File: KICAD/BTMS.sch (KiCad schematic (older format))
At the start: 314 parts, among them J1 fan, J10 U1COMMS, J11 U2COMMS, J13 IntBTemp, J14 ctrlTemp, J15 12Vout, J16 12Vin, J17 5Vout, J2 mContactor, J3 Tac, J5 ICSP, J7 5Vout, J9 key, Q1 PSMN5R6-100BS, Q10 PSMN5R6-100BS, Q11 DMN65D8L, Q12 DMN65D8L, Q13 FDN340P, Q14 ZXTP2025FTA, Q15 ZXTP2025FTA, Q16 ZXTP2025FTA, Q18 DMN65D8L, Q2 PSMN5R6-100BS, Q3 PSMN5R6-100BS, Q4 DMN65D8L, Q5 DMN65D8L, Q6 DMN65D8L, Q7 DMN65D8L, Q8 PSMN5R6-100BS, Q9 FDN340P, U1 R-78HB12-0.5, U10 A41AS12VDC, U11 A41AS12VDC, U12 A41AS12VDC, U13 A41AS12VDC, U14 A41AS12VDC, U15 NL17SZ74USG, U2 ACS780xLRTR-050B, U3 UCC27201DDAR, U4 FAN3111ESX, U5 HCPL-3120, U6 L7805CV, U7 LTV-817S, U8 dsPIC30F3011-PT, U9 LM62CIM3/NOPB

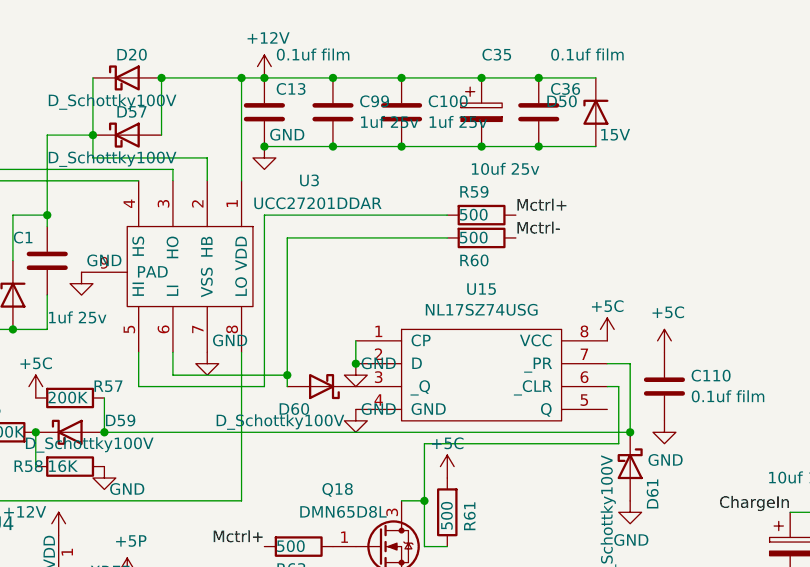
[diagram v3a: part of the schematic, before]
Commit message: Cleaned up a few things. Added mosfet to help protect against both high and low side fets from being on at the same time. Generated Gerber Files. Getting ready to fabricate this board and begin testing.
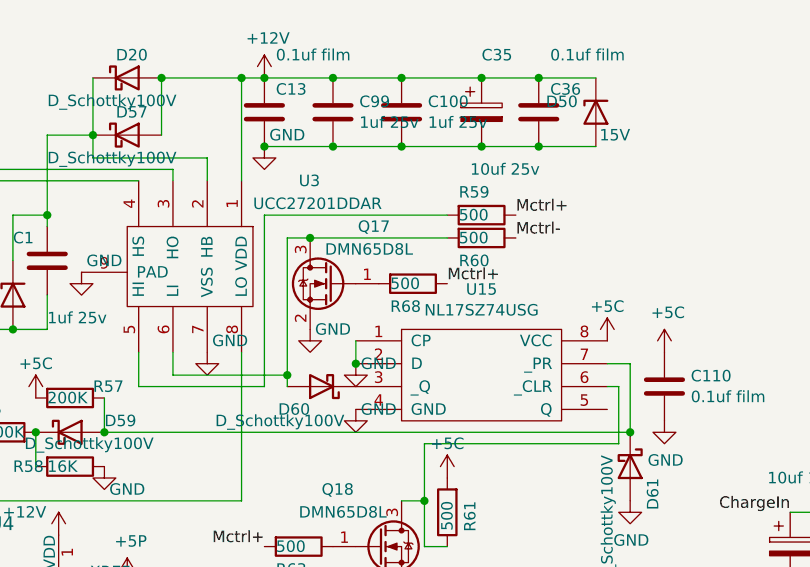
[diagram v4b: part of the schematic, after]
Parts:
- added Q17: DMN65D8L, TO_SOT_Packages_SMD:SOT-23, symbol Device:Q_NMOS_GSD
- added R68: 500, Resistors_SMD:R_0603, symbol Device:R
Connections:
- net GND: now also Q17.2 (S)
- net Mctrl+: now also R68.1
- net at D60.2 (A), R60.2, U3.6 (LI): now also Q17.3 (D)
- new net: Q17.1 (G), R68.2
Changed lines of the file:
@@
 	4650 6100 4650 5500
 Wire Wire Line
-	4650 5500 5350 5500
+	4650 5500 4750 5500
 Wire Wire Line
 	4550 5400 4550 6150
@@
 	4000 6150 4000 6000
 Wire Wire Line
-	4550 5400 5350 5400
-Wire Wire Line
 	4650 6150 4650 6100
 Connection ~ 4650 6100
+$Comp
+L Device:Q_NMOS_GSD Q17
+U 1 1 61CDE917
+P 4850 5700
+F 0 "Q17" H 4600 5950 50  0000 L CNN
+F 1 "DMN65D8L" H 4500 5850 50  0000 L CNN
+F 2 "TO_SOT_Packages_SMD:SOT-23" H 5050 5800 50  0001 C CNN
+F 3 "~" H 4850 5700 50  0001 C CNN
+F 4 "https://www.digikey.com/en/products/detail/diodes-incorporated/DMN65D8L-7/3678136" H 4850 5700 50  0001 C CNN "DK_Detail_Page"
+F 5 "DMN65D8L-7DICT-ND" H 4850 5700 50  0001 C CNN "Digi-Key_PN"
+	1    4850 5700
+	-1   0    0    -1
+$EndComp
+Connection ~ 4750 5500
+Wire Wire Line
+	4750 5500 5350 5500
+$Comp
+L power:GND #PWR0154
+U 1 1 61DF4C68
+P 4750 5900
+F 0 "#PWR0154" H 4750 5650 50  0001 C CNN
+F 1 "GND" H 4850 5900 50  0000 C CNN
+F 2 "" H 4750 5900 50  0001 C CNN
+F 3 "" H 4750 5900 50  0001 C CNN
+	1    4750 5900
+	1    0    0    -1
+$EndComp
+Wire Wire Line
+	4550 5400 5350 5400
+Text Label 5350 5700 0    50   ~ 0
+Mctrl+
+$Comp
+L Device:R R68
+U 1 1 61DFA87C
+P 5200 5700
+F 0 "R68" V 5300 5600 50  0000 L CNN
+F 1 "500" V 5200 5600 50  0000 L CNN
+F 2 "Resistors_SMD:R_0603" V 5130 5700 50  0001 C CNN
+F 3 "~" H 5200 5700 50  0001 C CNN
+F 4 "https://www.digikey.com/en/products/detail/stackpole-electronics-inc/RNCP0603FTD499R/2240098" H 5200 5700 50  0001 C CNN "DK_Detail_Page"
+F 5 "RNCP0603FTD499RCT-ND" H 5200 5700 50  0001 C CNN "Digi-Key_PN"
+	1    5200 5700
+	0    1    1    0
+$EndComp
 $EndSCHEMATC

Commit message: Added Digikey parts list. Ordered parts, but many critical parts are on  backorder so I will be reusing parts from the older prototypes that didn't explode.
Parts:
- R5: DK_Detail_Page https://www.digikey.com/en/products/detail/vishay-dale/CRCW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 -> https://www.digikey.com/en/products/detail/yageo/RC0603FR-0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; Digi-Key_PN 541-8.06SCT-ND -> 311-6.04HRCT-ND
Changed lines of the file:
@@
 F 2 "Resistors_SMD:R_0603" V 2330 5650 50  0001 C CNN
 F 3 "~" H 2400 5650 50  0001 C CNN
-F 4 "https://www.digikey.com/en/products/detail/vishay-dale/CRCW06038R06FKEAHP/2225948" H 2400 5650 50  0001 C CNN "DK_Detail_Page"
-F 5 "541-8.06SCT-ND" H 2400 5650 50  0001 C CNN "Digi-Key_PN"
+F 4 "https://www.digikey.com/en/products/detail/yageo/RC0603FR-076R04L/727316" H 2400 5650 50  0001 C CNN "DK_Detail_Page"
+F 5 "311-6.04HRCT-ND" H 2400 5650 50  0001 C CNN "Digi-Key_PN"
 	1    2400 5650
 	0    1    1    0

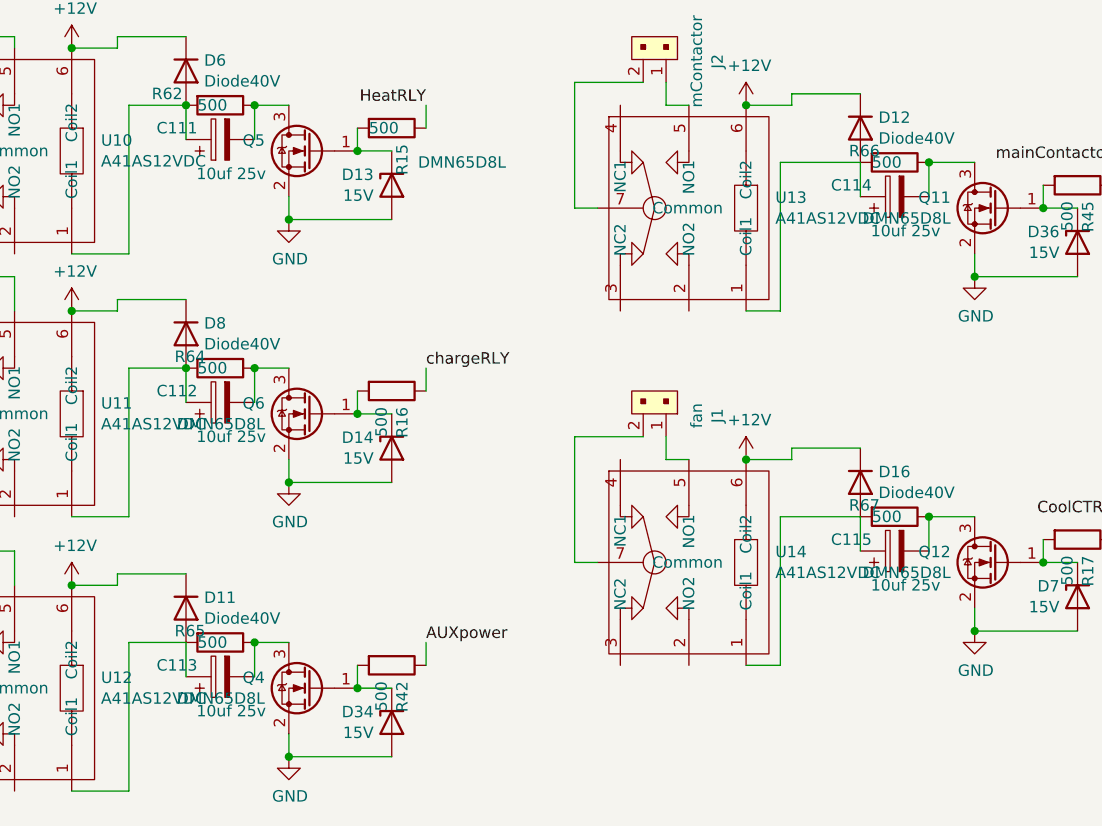
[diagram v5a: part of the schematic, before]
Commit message: Began board design bug fixes and upgrades. Began implementing vehicle speed calculation routines. Fixed a bug where system would power itself off 1 sec after unplugging charger. Fixed a bug where heater relay would not turn on/off during heat test and cal. Fixed a bug where AUX and mContactor relays would not turn on. Fixed a bug where system would hang when attempting to read fault codes.
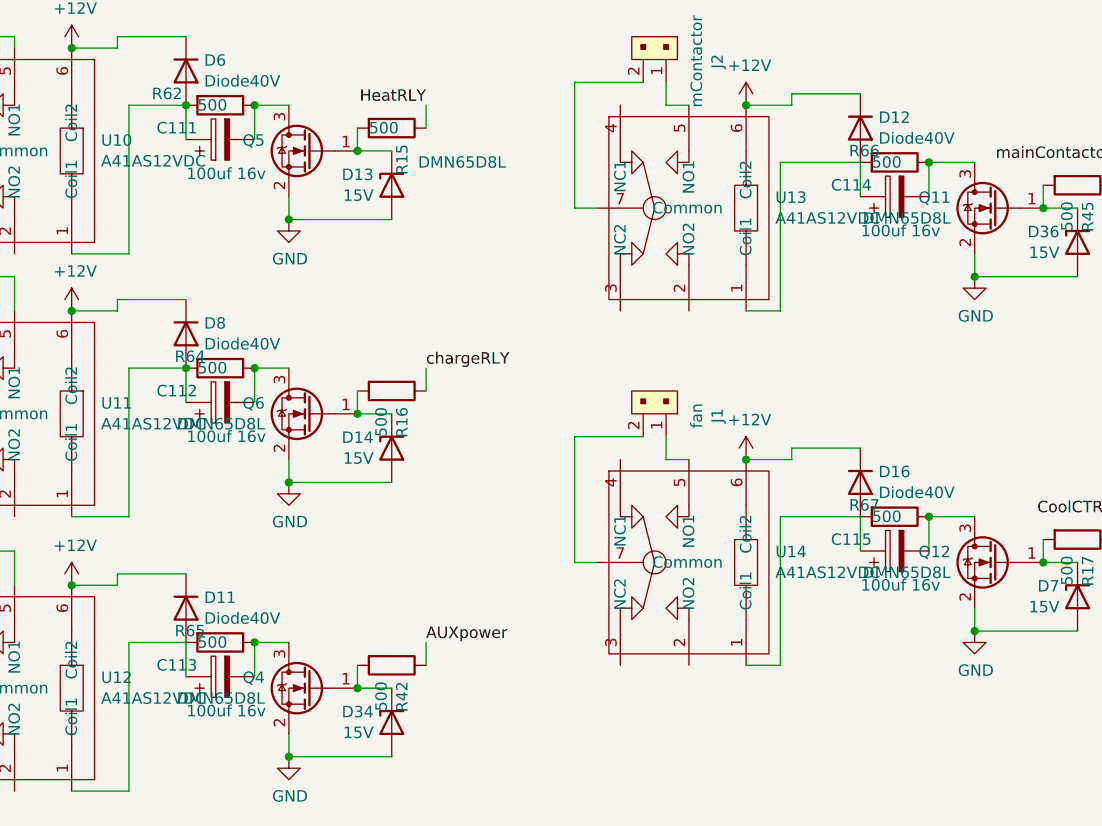
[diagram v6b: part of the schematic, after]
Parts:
- C111, C112, C113, C114, C115: value 10uf 25v -> 100uf 16v; footprint Capacitors_SMD:C_0805 -> Capacitors_SMD:CP_Elec_6.3x5.7; DK_Detail_Page https://www.digikey.com/en/products/detail/murata-electroni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 -> https://www.digikey.com/en/products/detail/illinois-capacit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; Digi-Key_PN 490-10748-1-ND -> 1572-1239-1-ND
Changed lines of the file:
@@
 P 2900 8300
 F 0 "C111" V 2950 8400 50  0000 L CNN
-F 1 "10uf 25v" V 2750 8100 50  0000 L CNN
-F 2 "Capacitors_SMD:C_0805" H 2938 8150 50  0001 C CNN
+F 1 "100uf 16v" V 2750 8100 50  0000 L CNN
+F 2 "Capacitors_SMD:CP_Elec_6.3x5.7" H 2938 8150 50  0001 C CNN
 F 3 "~" H 2900 8300 50  0001 C CNN
-F 4 "https://www.digikey.com/en/products/detail/murata-electronics/GRM21BR61E106MA73L/5251352" H 2900 8300 50  0001 C CNN "DK_Detail_Page"
-F 5 "490-10748-1-ND" H 2900 8300 50  0001 C CNN "Digi-Key_PN"
+F 4 "https://www.digikey.com/en/products/detail/illinois-capacitor/107AXZ016MQ5/5964380" H 2900 8300 50  0001 C CNN "DK_Detail_Page"
+F 5 "1572-1239-1-ND" H 2900 8300 50  0001 C CNN "Digi-Key_PN"
 	1    2900 8300
 	0    -1   -1   0
@@
 	0    1    1    0
 $EndComp
-$Comp
-L Device:CP C112
-U 1 1 611D0654
-P 2900 9450
-F 0 "C112" V 2950 9550 50  0000 L CNN
-F 1 "10uf 25v" V 2750 9250 50  0000 L CNN
-F 2 "Capacitors_SMD:C_0805" H 2938 9300 50  0001 C CNN
-F 3 "~" H 2900 9450 50  0001 C CNN
-F 4 "https://www.digikey.com/en/products/detail/murata-electronics/GRM21BR61E106MA73L/5251352" H 2900 9450 50  0001 C CNN "DK_Detail_Page"
-F 5 "490-10748-1-ND" H 2900 9450 50  0001 C CNN "Digi-Key_PN"
-	1    2900 9450
-	0    -1   -1   0
-$EndComp
 Wire Wire Line
 	3050 9300 3050 9450
@@
 	0    1    1    0
 $EndComp
-$Comp
-L Device:CP C113
-U 1 1 61467AFD
-P 2900 10650
-F 0 "C113" V 2950 10750 50  0000 L CNN
-F 1 "10uf 25v" V 2750 10450 50  0000 L CNN
-F 2 "Capacitors_SMD:C_0805" H 2938 10500 50  0001 C CNN
-F 3 "~" H 2900 10650 50  0001 C CNN
-F 4 "https://www.digikey.com/en/products/detail/murata-electronics/GRM21BR61E106MA73L/5251352" H 2900 10650 50  0001 C CNN "DK_Detail_Page"
-F 5 "490-10748-1-ND" H 2900 10650 50  0001 C CNN "Digi-Key_PN"
-	1    2900 10650
-	0    -1   -1   0
-$EndComp
 Wire Wire Line
 	3050 10500 3050 10650
@@
 	0    1    1    0
 $EndComp
-$Comp
-L Device:CP C114
-U 1 1 615F924D
-P 5850 8550
-F 0 "C114" V 5900 8650 50  0000 L CNN
-F 1 "10uf 25v" V 5700 8350 50  0000 L CNN
-F 2 "Capacitors_SMD:C_0805" H 5888 8400 50  0001 C CNN
-F 3 "~" H 5850 8550 50  0001 C CNN
-F 4 "https://www.digikey.com/en/products/detail/murata-electronics/GRM21BR61E106MA73L/5251352" H 5850 8550 50  0001 C CNN "DK_Detail_Page"
-F 5 "490-10748-1-ND" H 5850 8550 50  0001 C CNN "Digi-Key_PN"
-	1    5850 8550
-	0    -1   -1   0
-$EndComp
 Wire Wire Line
 	6000 8400 6000 8550
@@
 	1    5850 9950
 	0    1    1    0
-$EndComp
-$Comp
-L Device:CP C115
-U 1 1 6178E7F0
-P 5850 10100
-F 0 "C115" V 5900 10200 50  0000 L CNN
-F 1 "10uf 25v" V 5700 9900 50  0000 L CNN
-F 2 "Capacitors_SMD:C_0805" H 5888 9950 50  0001 C CNN
-F 3 "~" H 5850 10100 50  0001 C CNN
-F 4 "https://www.digikey.com/en/products/detail/murata-electronics/GRM21BR61E106MA73L/5251352" H 5850 10100 50  0001 C CNN "DK_Detail_Page"
-F 5 "490-10748-1-ND" H 5850 10100 50  0001 C CNN "Digi-Key_PN"
-	1    5850 10100
-	0    -1   -1   0
 $EndComp
 Wire Wire Line
@@
 	0    1    1    0
 $EndComp
+$Comp
+L Device:CP C112
+U 1 1 62113170
+P 2900 9450
+F 0 "C112" V 2950 9550 50  0000 L CNN
+F 1 "100uf 16v" V 2750 9250 50  0000 L CNN
+F 2 "Capacitors_SMD:CP_Elec_6.3x5.7" H 2938 9300 50  0001 C CNN
+F 3 "~" H 2900 9450 50  0001 C CNN
+F 4 "https://www.digikey.com/en/products/detail/illinois-capacitor/107AXZ016MQ5/5964380" H 2900 9450 50  0001 C CNN "DK_Detail_Page"
+F 5 "1572-1239-1-ND" H 2900 9450 50  0001 C CNN "Digi-Key_PN"
+	1    2900 9450
+	0    -1   -1   0
+$EndComp
+$Comp
+L Device:CP C113
+U 1 1 62113BDC
+P 2900 10650
+F 0 "C113" V 2950 10750 50  0000 L CNN
+F 1 "100uf 16v" V 2750 10450 50  0000 L CNN
+F 2 "Capacitors_SMD:CP_Elec_6.3x5.7" H 2938 10500 50  0001 C CNN
+F 3 "~" H 2900 10650 50  0001 C CNN
+F 4 "https://www.digikey.com/en/products/detail/illinois-capacitor/107AXZ016MQ5/5964380" H 2900 10650 50  0001 C CNN "DK_Detail_Page"
+F 5 "1572-1239-1-ND" H 2900 10650 50  0001 C CNN "Digi-Key_PN"
+	1    2900 10650
+	0    -1   -1   0
+$EndComp
+$Comp
+L Device:CP C115
+U 1 1 62114193
+P 5850 10100
+F 0 "C115" V 5900 10200 50  0000 L CNN
+F 1 "100uf 16v" V 5700 9900 50  0000 L CNN
+F 2 "Capacitors_SMD:CP_Elec_6.3x5.7" H 5888 9950 50  0001 C CNN
+F 3 "~" H 5850 10100 50  0001 C CNN
+F 4 "https://www.digikey.com/en/products/detail/illinois-capacitor/107AXZ016MQ5/5964380" H 5850 10100 50  0001 C CNN "DK_Detail_Page"
+F 5 "1572-1239-1-ND" H 5850 10100 50  0001 C CNN "Digi-Key_PN"
+	1    5850 10100
+	0    -1   -1   0
+$EndComp
+$Comp
+L Device:CP C114
+U 1 1 62114F09
+P 5850 8550
+F 0 "C114" V 5900 8650 50  0000 L CNN
+F 1 "100uf 16v" V 5700 8350 50  0000 L CNN
+F 2 "Capacitors_SMD:CP_Elec_6.3x5.7" H 5888 8400 50  0001 C CNN
+F 3 "~" H 5850 8550 50  0001 C CNN
+F 4 "https://www.digikey.com/en/products/detail/illinois-capacitor/107AXZ016MQ5/5964380" H 5850 8550 50  0001 C CNN "DK_Detail_Page"
+F 5 "1572-1239-1-ND" H 5850 8550 50  0001 C CNN "Digi-Key_PN"
+	1    5850 8550
+	0    -1   -1   0
+$EndComp
 $EndSCHEMATC

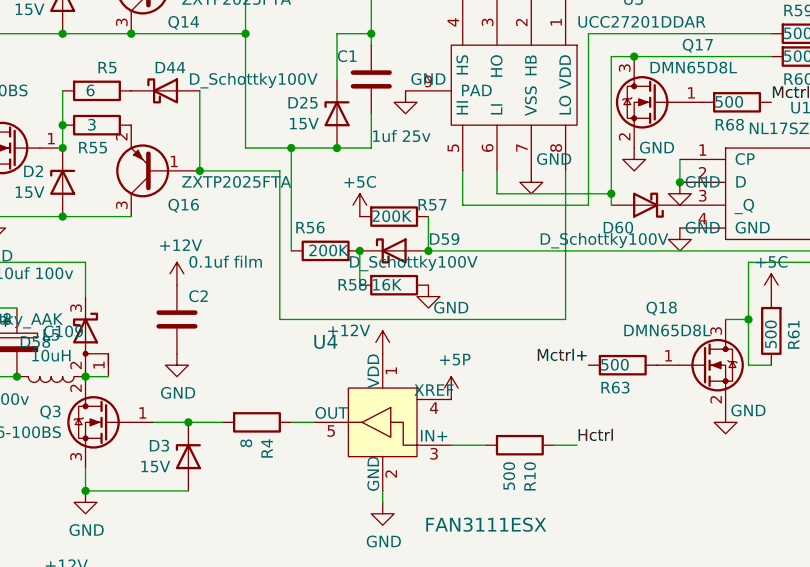
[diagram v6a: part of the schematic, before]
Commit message: Removed R58 from circuit design; not needed. Changed firmware to use built in dead time generator and verified that the High and Low differential pair is configured correctly. Circuit seems to work as intended under no load. Need to test under load.
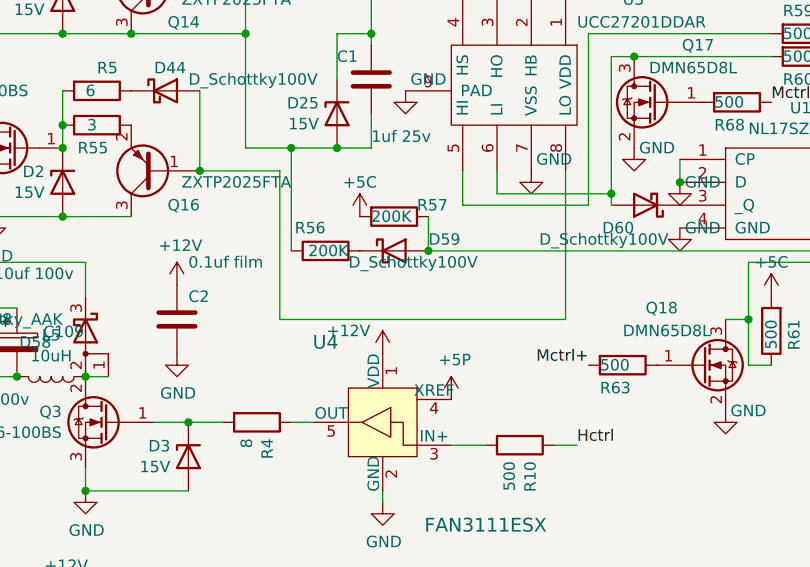
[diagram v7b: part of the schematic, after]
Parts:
- removed R58: 16K, Resistors_SMD:R_0603, symbol Device:R
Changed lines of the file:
@@
-$EndComp
-$Comp
-L Device:R R58
-U 1 1 6056FD16
-P 3700 6500
-F 0 "R58" V 3700 6250 50  0000 L CNN
-F 1 "16K" V 3700 6400 50  0000 L CNN
-F 2 "Resistors_SMD:R_0603" V 3630 6500 50  0001 C CNN
-F 3 "~" H 3700 6500 50  0001 C CNN
-F 4 "https://www.digikey.com/en/products/detail/vishay-dale/CRCW060316K0FKEAHP/2226306" H 3700 6500 50  0001 C CNN "DK_Detail_Page"
-F 5 "541-CRCW060316K0FKEAHPCT-ND" H 3700 6500 50  0001 C CNN "Digi-Key_PN"
-	1    3700 6500
-	0    1    1    0
 $EndComp
 $Comp
@@
 	1    3400 6350
 	0    -1   -1   0
-$EndComp
-$Comp
-L power:GND #PWR0143
-U 1 1 6056FD24
-P 3850 6500
-F 0 "#PWR0143" H 3850 6250 50  0001 C CNN
-F 1 "GND" H 3950 6400 50  0000 C CNN
-F 2 "" H 3850 6500 50  0001 C CNN
-F 3 "" H 3850 6500 50  0001 C CNN
-	1    3850 6500
-	1    0    0    -1
 $EndComp
 $Comp
@@
 	1    0    0    -1
 $EndComp
-Connection ~ 3550 6350
 Wire Wire Line
 	3850 6200 3850 6350
 Wire Wire Line
-	3550 6350 3550 6500
-Wire Wire Line
 	3250 6350 3250 5900
